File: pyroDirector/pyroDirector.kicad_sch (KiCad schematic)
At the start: 35 parts, among them J1 Conn_01x03_Male, J10 BTNS, J11 DC_Conv, J12 CALIB_MODULE, J13 DISP_I2C, J2 AudioJack3.5mm, J3 Header_A1-A15, J4 Header_D14-19_D49_51_53, J6 V_Batt, J7 Header_ISP, J8 PWR_SWITCH, J9 Batt, Q1 MMBT2222A 1P, SW1 SW_Enable, U1 MEGA_PRO_ATMEGA2560

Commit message: Manufactured 2021-02-25
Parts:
- C1: LCSC (none) -> C49678
- Q1: LCSC (none) -> C8512
- R1, R2, R3: LCSC (none) -> C17514
- R4, R5: LCSC (none) -> C17673
- S1, S2, S3, S6: LCSC (none) -> C318884
- S4: value PCB_Btn_OK -> PCB_Btn_LEFT; LCSC (none) -> C318884
- S5: value PCB_Btn_OK -> PCB_Btn_RIGHT; LCSC (none) -> C318884
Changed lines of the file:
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@@
+      (effects (font (size 1.27 1.27)) hide)
+    )
+    (property "LCSC" "C318884" (id 9) (at 97.79 132.08 0)
       (effects (font (size 1.27 1.27)) hide)
     )
@@
       (effects (font (size 1.27 1.27)) hide)
     )
+    (property "LCSC" "C17514" (id 4) (at 19.05 43.18 0)
+      (effects (font (size 1.27 1.27)) hide)
+    )
     (pin "1")
     (pin "2")
@@
       (effects (font (size 1.27 1.27)) (justify left))
     )
-    (property "Value" "PCB_Btn_OK" (id 1) (at 165.1 124.46 0)
+    (property "Value" "PCB_Btn_RIGHT" (id 1) (at 165.1 124.46 0)
       (effects (font (size 1.27 1.27)) (justify left))
     )
@@
     )
     (property "DISPNAME" "JLC Basic Btn" (id 8) (at 165.1 132.08 0)
+      (effects (font (size 1.27 1.27)) hide)
+    )
+    (property "LCSC" "C318884" (id 9) (at 168.91 132.08 0)
       (effects (font (size 1.27 1.27)) hide)
     )
@@
     (property "Datasheet" "~" (id 3) (at 29.21 63.5 0)
       (effects (font (size 1.27 1.27)) hide)
+    )
+    (property "LCSC" "C49678" (id 4) (at 29.21 63.5 0)
+      (effects (font (size 0 0)) hide)
     )
     (pin "1")
@@
       (effects (font (size 1.27 1.27)) hide)
     )
+    (property "LCSC" "C17514" (id 4) (at 19.05 53.34 0)
+      (effects (font (size 1.27 1.27)) hide)
+    )
     (pin "1")
     (pin "2")
@@
     )
     (property "DISPNAME" "JLC Basic Btn" (id 8) (at 187.96 132.08 0)
+      (effects (font (size 1.27 1.27)) hide)
+    )
+    (property "LCSC" "C318884" (id 9) (at 191.77 132.08 0)
       (effects (font (size 1.27 1.27)) hide)
     )
@@
       (effects (font (size 1.27 1.27)) hide)
     )
+    (property "LCSC" "C17673" (id 4) (at 45.72 99.06 90)
+      (effects (font (size 1.27 1.27)) hide)
+    )
     (pin "1")
     (pin "2")
@@
       (effects (font (size 1.27 1.27)) (justify left))
     )
-    (property "Value" "PCB_Btn_OK" (id 1) (at 142.24 124.46 0)
+    (property "Value" "PCB_Btn_LEFT" (id 1) (at 142.24 124.46 0)
       (effects (font (size 1.27 1.27)) (justify left))
     )
@@
     )
     (property "DISPNAME" "JLC Basic Btn" (id 8) (at 142.24 132.08 0)
+      (effects (font (size 1.27 1.27)) hide)
+    )
+    (property "LCSC" "C318884" (id 9) (at 146.05 132.08 0)
       (effects (font (size 1.27 1.27)) hide)
     )
@@
     )
     (property "Datasheet" "~" (id 3) (at 45.72 114.3 0)
+      (effects (font (size 1.27 1.27)) hide)
+    )
+    (property "LCSC" "C17673" (id 4) (at 45.72 114.3 90)
       (effects (font (size 1.27 1.27)) hide)
     )
@@
       (effects (font (size 1.27 1.27)) hide)
     )
+    (property "LCSC" "C318884" (id 9) (at 73.66 132.08 0)
+      (effects (font (size 1.27 1.27)) hide)
+    )
     (pin "A")
     (pin "B")
@@
       (effects (font (size 1.27 1.27)) hide)
     )
+    (property "LCSC" "C318884" (id 9) (at 123.19 132.08 0)
+      (effects (font (size 1.27 1.27)) hide)
+    )
     (pin "A")
     (pin "B")
@@
       (effects (font (size 1.27 1.27)) hide)
     )
+    (property "LCSC" "C17514" (id 4) (at 19.05 63.5 0)
+      (effects (font (size 1.27 1.27)) hide)
+    )
     (pin "1")
     (pin "2")
@@
     (property "Datasheet" "https://datasheet.lcsc.com/lcsc/1811081957_Jiangsu-Changjing-Electronics-Technology-Co---Ltd--MMBT2222A-1P_C8512.pdf" (id 3) (at 30.48 102.87 0)
       (effects (font (size 1.27 1.27)) (justify left) hide)
+    )
+    (property "LCSC" "C8512" (id 4) (at 36.83 99.06 0)
+      (effects (font (size 1.27 1.27)) hide)
     )
     (pin "1")
@@
     )
     (path "/458428d3-b6de-404e-801a-df880e8758bb/f41d24b1-cbcc-4418-88a6-6e3216a25102"
-      (reference "D1") (unit 1) (value "SM4007") (footprint "Diode_SMD:D_SMA")
+      (reference "D1") (unit 1) (value "M7") (footprint "Diode_SMD:D_SMA")
     )
     (path "/4c7b0061-a421-432d-8542-cfa6f0e5e1a1/f41d24b1-cbcc-4418-88a6-6e3216a25102"
-      (reference "D2") (unit 1) (value "SM4007") (footprint "Diode_SMD:D_SMA")
+      (reference "D2") (unit 1) (value "M7") (footprint "Diode_SMD:D_SMA")
     )
     (path "/ec591659-430a-4a08-bf8a-ecb93b991ef2/f41d24b1-cbcc-4418-88a6-6e3216a25102"
-      (reference "D3") (unit 1) (value "SM4007") (footprint "Diode_SMD:D_SMA")
+      (reference "D3") (unit 1) (value "M7") (footprint "Diode_SMD:D_SMA")
     )
     (path "/4ff4b4e5-f8d6-4345-a01d-697b4f25b291"
@@
     )
     (path "/ae6f20f9-fa6e-4a4c-872a-2bdcbf5cb2b8"
-      (reference "S4") (unit 1) (value "PCB_Btn_OK") (footprint "TS-1187A-B-A-B:SW_TS-1187A-B-A-B")
+      (reference "S4") (unit 1) (value "PCB_Btn_LEFT") (footprint "TS-1187A-B-A-B:SW_TS-1187A-B-A-B")
     )
     (path "/1b19488b-5a82-4063-8df4-bd8cd5fb83dc"
-      (reference "S5") (unit 1) (value "PCB_Btn_OK") (footprint "TS-1187A-B-A-B:SW_TS-1187A-B-A-B")
+      (reference "S5") (unit 1) (value "PCB_Btn_RIGHT") (footprint "TS-1187A-B-A-B:SW_TS-1187A-B-A-B")
     )
     (path "/58d97bc8-1719-4033-87b4-26233386e667"

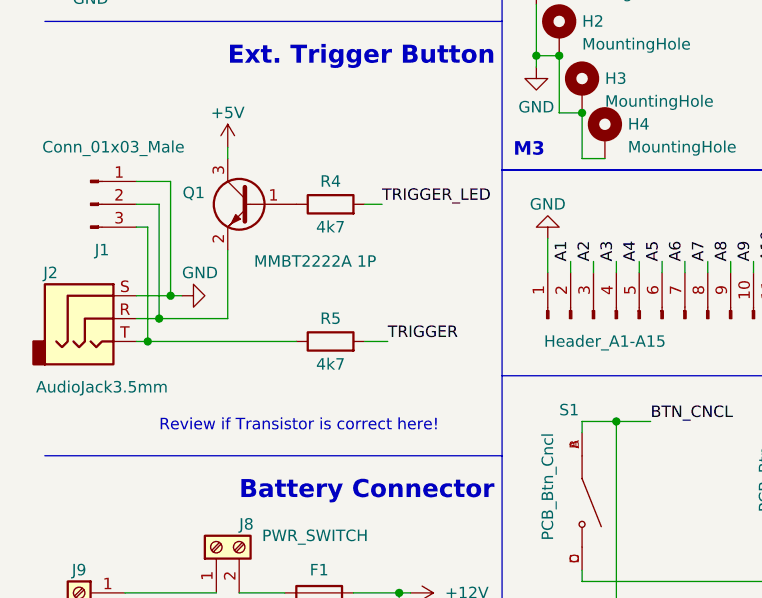
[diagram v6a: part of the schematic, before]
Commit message: replaced trigger transistor with PNP variant
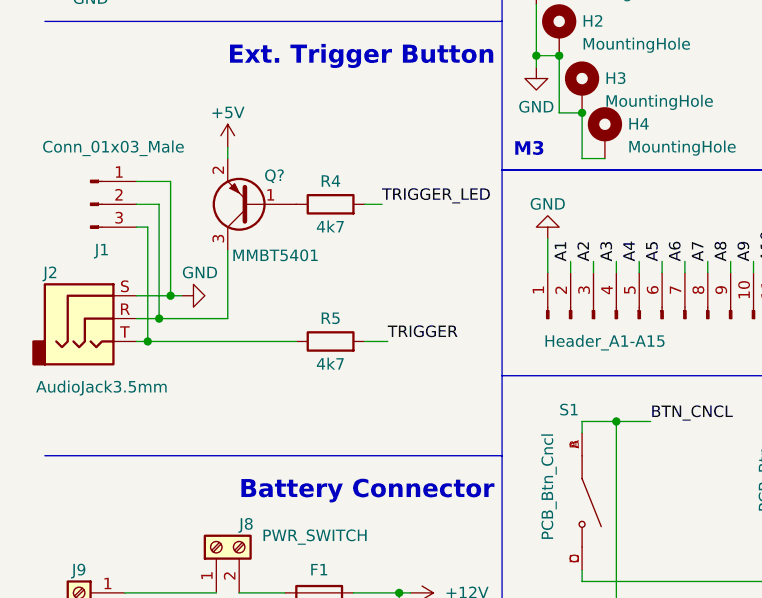
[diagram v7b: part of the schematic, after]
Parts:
- removed Q1: MMBT2222A 1P, Package_TO_SOT_SMD:SOT-23, symbol JLCPCB_Parts:MMBT2222A 1P
- added Q?: MMBT5401, Package_TO_SOT_SMD:SOT-23, symbol Transistor_BJT:BC807
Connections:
- net +5V: now also Q?.2 (E)
- net at J1.2 (Pin_2), J2.R: now also Q?.3 (C)
- net at R4.1: now also Q?.1 (B)
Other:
- note removed: "Review if Transistor is correct here!"
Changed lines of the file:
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@@
     (stroke (width 0) (type default) (color 0 0 0 0))
-  )
-  (text "Review if Transistor is correct here!" (at 26.67 124.46 0)
-    (effects (font (size 1.27 1.27)) (justify left bottom))
   )
   (text "PyroDirector" (at 15.24 22.86 0)
@@
     (pin "3")
   )
-  (symbol (lib_id "JLCPCB_Parts:MMBT2222A 1P") (at 36.83 99.06 0) (mirror y) (unit 1)
-    (in_bom yes) (on_board yes)
-    (property "Reference" "Q1" (id 0) (at 31.75 97.7899 0)
-      (effects (font (size 1.27 1.27)) (justify left))
-    )
-    (property "Value" "MMBT2222A 1P" (id 1) (at 50.8 105.41 0)
-      (effects (font (size 1.27 1.27)) (justify left))
-    )
-    (property "Footprint" "Package_TO_SOT_SMD:SOT-23" (id 2) (at 30.48 105.41 0)
-      (effects (font (size 1.27 1.27) italic) (justify left) hide)
-    )
-    (property "Datasheet" "https://datasheet.lcsc.com/lcsc/1811081957_Jiangsu-Changjing-Electronics-Technology-Co---Ltd--MMBT2222A-1P_C8512.pdf" (id 3) (at 30.48 102.87 0)
-      (effects (font (size 1.27 1.27)) (justify left) hide)
-    )
-    (property "LCSC" "C8512" (id 4) (at 36.83 99.06 0)
-      (effects (font (size 1.27 1.27)) hide)
-    )
-    (pin "1")
-    (pin "2")
-    (pin "3")
-  )
   (symbol (lib_id "Connector:Screw_Terminal_01x02") (at 17.78 142.24 0) (mirror y) (unit 1)
     (in_bom yes) (on_board yes)
@@
     (pin "1")
     (pin "2")
+  )
+  (symbol (lib_id "Transistor_BJT:BC807") (at 36.83 99.06 180) (unit 1)
+    (in_bom yes) (on_board yes)
+    (property "Reference" "Q?" (id 0) (at 40.64 95.885 0)
+      (effects (font (size 1.27 1.27)) (justify left))
+    )
+    (property "Value" "MMBT5401" (id 1) (at 44.45 104.775 0)
+      (effects (font (size 1.27 1.27)) (justify left))
+    )
+    (property "Footprint" "Package_TO_SOT_SMD:SOT-23" (id 2) (at 31.75 97.155 0)
+      (effects (font (size 1.27 1.27) italic) (justify left) hide)
+    )
+    (property "Datasheet" "https://www.onsemi.com/pub/Collateral/BC808-D.pdf" (id 3) (at 36.83 99.06 0)
+      (effects (font (size 1.27 1.27)) (justify left) hide)
+    )
+    (pin "1")
+    (pin "2")
+    (pin "3")
   )
   (symbol (lib_id "power:+5V") (at 147.32 102.87 0) (unit 1)
@@
       (reference "K3") (unit 1) (value "PR12-5V-360-1C") (footprint "CUI Relays:PR12-5V-360-1C")
     )
-    (path "/ef5f9ca5-2216-4ab4-a7bd-8201a534beae"
-      (reference "Q1") (unit 1) (value "MMBT2222A 1P") (footprint "Package_TO_SOT_SMD:SOT-23")
-    )
     (path "/b00547c4-0dc8-4b78-a3cf-490ec0dbf130/3fdd5b8f-f4a2-4b81-82a2-372cd9ac6841"
       (reference "Q2") (unit 1) (value "MMBT2222A 1P") (footprint "Package_TO_SOT_SMD:SOT-23")
@@
       (reference "Q13") (unit 1) (value "IRLB8721PbF") (footprint "Package_TO_SOT_THT:TO-220-3_Vertical")
     )
+    (path "/f1c3eaf8-13f0-475e-93dd-a7652e32b312"
+      (reference "Q?") (unit 1) (value "MMBT5401") (footprint "Package_TO_SOT_SMD:SOT-23")
+    )
     (path "/0faa22ea-740e-43a5-aa64-13094eb844dc"
